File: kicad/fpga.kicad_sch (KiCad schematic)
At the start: 55 parts, among them J3 TC2050 JTAG, J4 SMA 10MHz REF, J5 PMOD0, J6 PMOD1, U10 W25Q128JVSIQ, U12 LFE5U-25F-6BG256C, U14 74LVC1G17

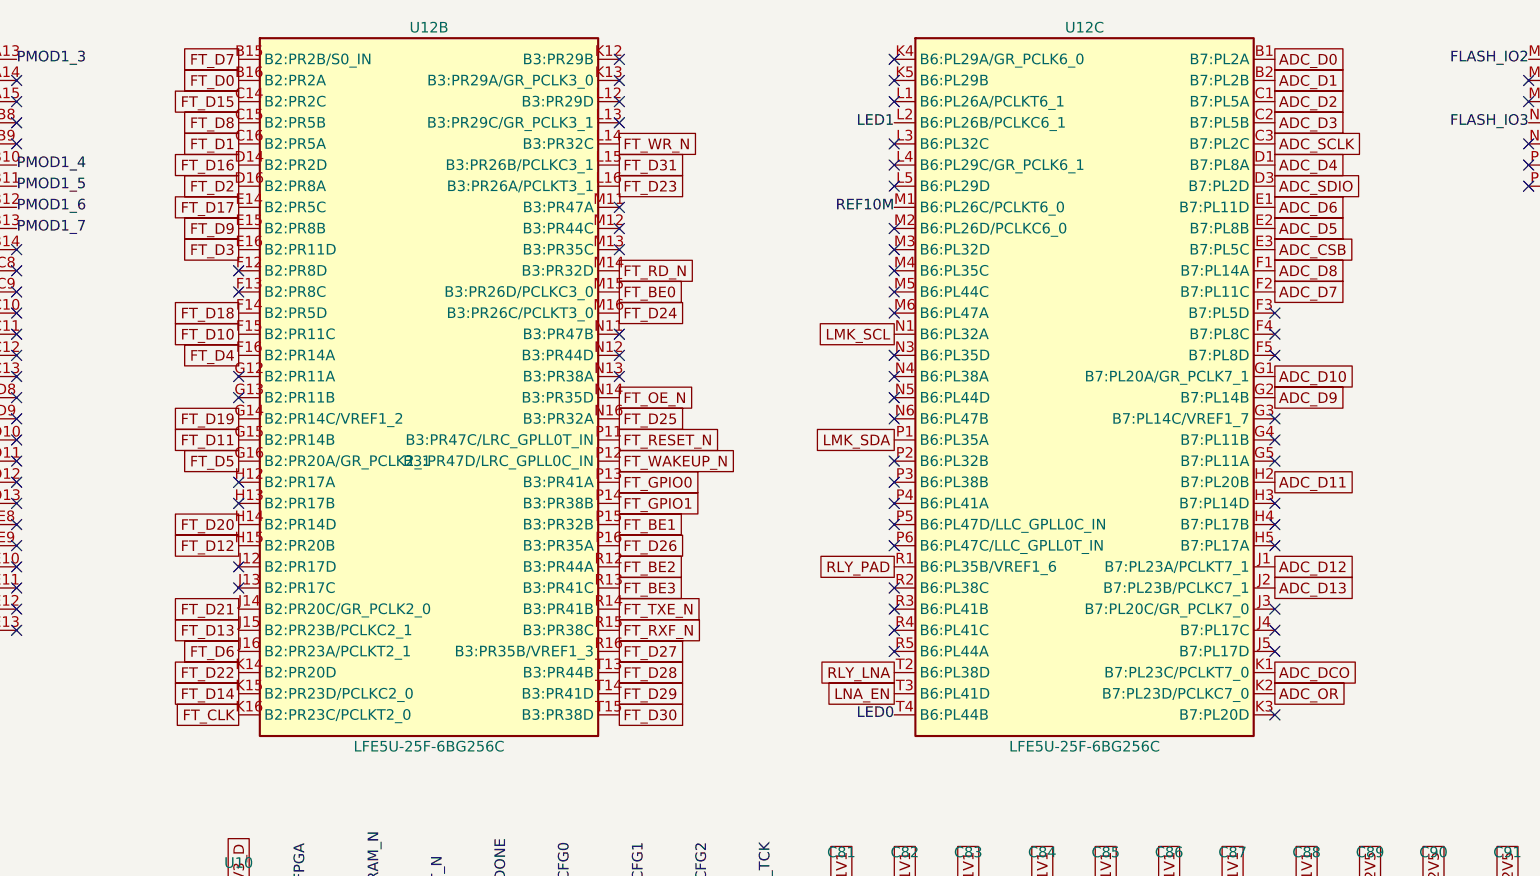
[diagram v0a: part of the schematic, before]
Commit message: Bus pin swap, FT601 IO registers, ADC clock layout, working board and fan-out tooling
- FPGA ball re-assignment (AGY, verified): FT601 and ADC buses planar; LPF, design.py, schematic, netlist synced.
- Gateware: FT601 outputs/tristates in IOLOGIC on a +112.5 deg PLL clock; AD9649 DCO inverted at boot.
- ADC sample clock laid out on F.Cu with swapped polarity; BOM U9 corrected to the 8-pin I2C LMK61E2.
- kicad/work: DeepPCB run 2 board plus scripted patches (buck, In2 GND fill, VCCAUX, clock); DeepPCB snapshots.
- kicad/gen: patch, repair, routing and fan-out scripts (fanout_apply, fanout_trial, place_free, escape_apply).
- notes/pinswap, notes/fanout: briefs, AGY results and Claude's reviews.
- Vendor datasheets removed from the repo; refs/datasheets.md lists their sources.

Co-Authored-By: Claude Opus 5.5 <noreply@anthropic.com>
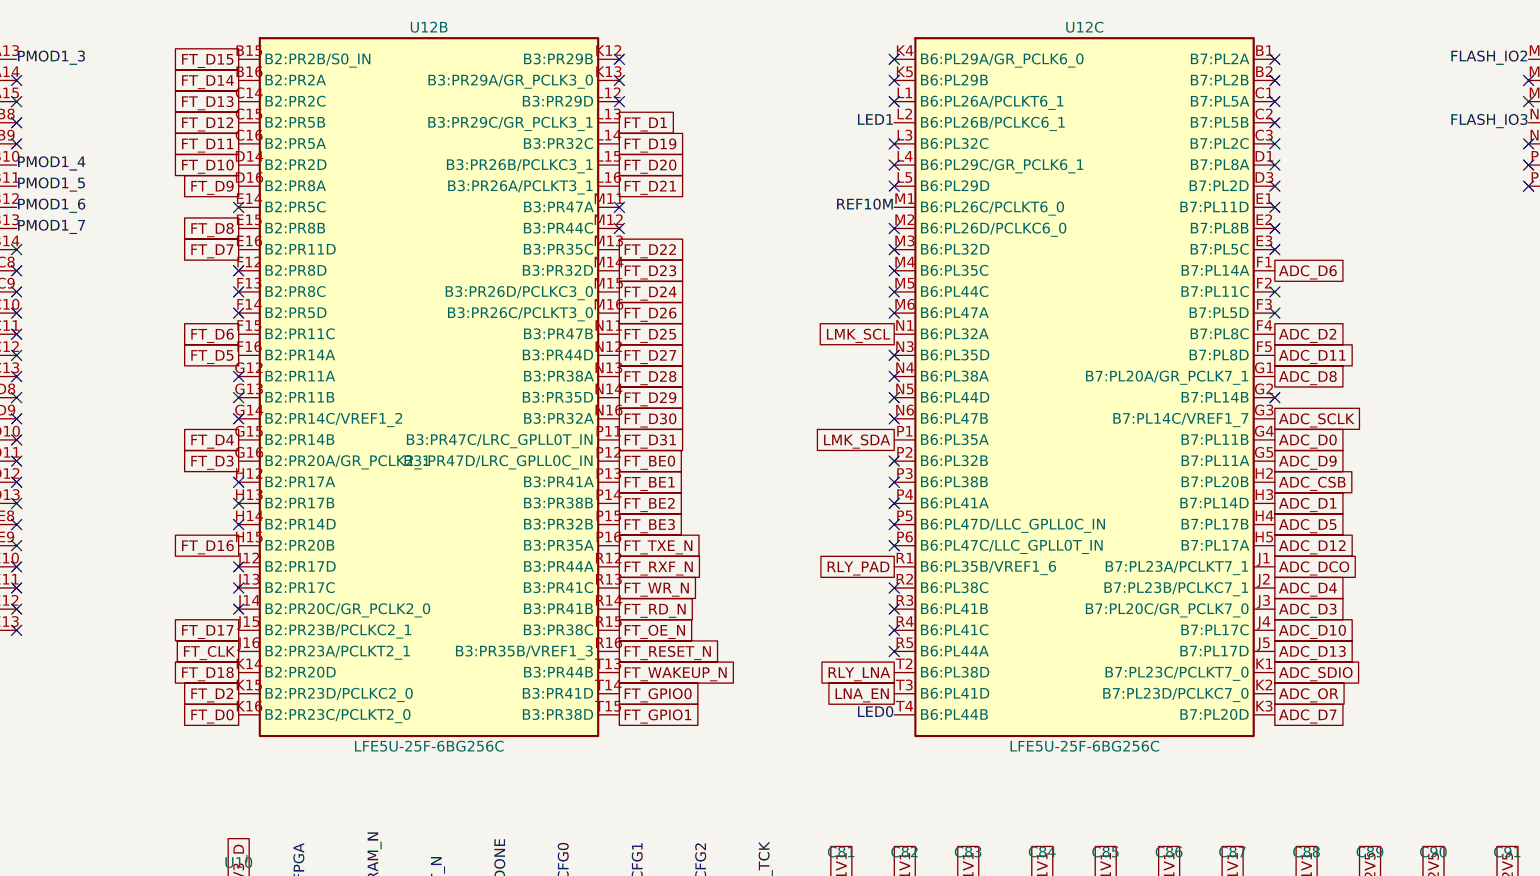
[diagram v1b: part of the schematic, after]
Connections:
- net ADC_CSB: now also U12.H2 (B7:PL20B); no longer U12.E3 (B7:PL5C)
- net ADC_D0: now also U12.G4 (B7:PL11B); no longer U12.B1 (B7:PL2A)
- net ADC_D1: now also U12.H3 (B7:PL14D); no longer U12.B2 (B7:PL2B)
- net ADC_D10: now also U12.J4 (B7:PL17C); no longer U12.G1 (B7:PL20A/GR_PCLK7_1)
- net ADC_D11: now also U12.F5 (B7:PL8D); no longer U12.H2 (B7:PL20B)
- net ADC_D12: now also U12.H5 (B7:PL17A); no longer U12.J1 (B7:PL23A/PCLKT7_1)
- net ADC_D13: now also U12.J5 (B7:PL17D); no longer U12.J2 (B7:PL23B/PCLKC7_1)
- net ADC_D2: now also U12.F4 (B7:PL8C); no longer U12.C1 (B7:PL5A)
- net ADC_D3: now also U12.J3 (B7:PL20C/GR_PCLK7_0); no longer U12.C2 (B7:PL5B)
- net ADC_D4: now also U12.J2 (B7:PL23B/PCLKC7_1); no longer U12.D1 (B7:PL8A)
- net ADC_D5: now also U12.H4 (B7:PL17B); no longer U12.E2 (B7:PL8B)
- net ADC_D6: now also U12.F1 (B7:PL14A); no longer U12.E1 (B7:PL11D)
- net ADC_D7: now also U12.K3 (B7:PL20D); no longer U12.F2 (B7:PL11C)
- net ADC_D8: now also U12.G1 (B7:PL20A/GR_PCLK7_1); no longer U12.F1 (B7:PL14A)
- net ADC_D9: now also U12.G5 (B7:PL11A); no longer U12.G2 (B7:PL14B)
- net ADC_DCO: now also U12.J1 (B7:PL23A/PCLKT7_1); no longer U12.K1 (B7:PL23C/PCLKT7_0)
- net ADC_SCLK: now also U12.G3 (B7:PL14C/VREF1_7); no longer U12.C3 (B7:PL2C)
- net ADC_SDIO: now also U12.K1 (B7:PL23C/PCLKT7_0); no longer U12.D3 (B7:PL2D)
- net FT_BE0: now also U12.P12 (B3:PR47D/LRC_GPLL0C_IN); no longer U12.M15 (B3:PR26D/PCLKC3_0)
- net FT_BE1: now also U12.P13 (B3:PR41A); no longer U12.P15 (B3:PR32B)
- net FT_BE2: now also U12.P14 (B3:PR38B); no longer U12.R12 (B3:PR44A)
- net FT_BE3: now also U12.P15 (B3:PR32B); no longer U12.R13 (B3:PR41C)
- net FT_CLK: now also U12.J16 (B2:PR23A/PCLKT2_1); no longer U12.K16 (B2:PR23C/PCLKT2_0)
- net FT_D0: now also U12.K16 (B2:PR23C/PCLKT2_0); no longer U12.B16 (B2:PR2A)
- net FT_D1: now also U12.L13 (B3:PR29C/GR_PCLK3_1); no longer U12.C16 (B2:PR5A)
- net FT_D10: now also U12.D14 (B2:PR2D); no longer U12.F15 (B2:PR11C)
- net FT_D11: now also U12.C16 (B2:PR5A); no longer U12.G15 (B2:PR14B)
- net FT_D12: now also U12.C15 (B2:PR5B); no longer U12.H15 (B2:PR20B)
- net FT_D13: now also U12.C14 (B2:PR2C); no longer U12.J15 (B2:PR23B/PCLKC2_1)
- net FT_D14: now also U12.B16 (B2:PR2A); no longer U12.K15 (B2:PR23D/PCLKC2_0)
- net FT_D15: now also U12.B15 (B2:PR2B/S0_IN); no longer U12.C14 (B2:PR2C)
- net FT_D16: now also U12.H15 (B2:PR20B); no longer U12.D14 (B2:PR2D)
- net FT_D17: now also U12.J15 (B2:PR23B/PCLKC2_1); no longer U12.E14 (B2:PR5C)
- net FT_D18: now also U12.K14 (B2:PR20D); no longer U12.F14 (B2:PR5D)
- net FT_D19: now also U12.L14 (B3:PR32C); no longer U12.G14 (B2:PR14C/VREF1_2)
- net FT_D2: now also U12.K15 (B2:PR23D/PCLKC2_0); no longer U12.D16 (B2:PR8A)
- net FT_D20: now also U12.L15 (B3:PR26B/PCLKC3_1); no longer U12.H14 (B2:PR14D)
- net FT_D21: now also U12.L16 (B3:PR26A/PCLKT3_1); no longer U12.J14 (B2:PR20C/GR_PCLK2_0)
- net FT_D22: now also U12.M13 (B3:PR35C); no longer U12.K14 (B2:PR20D)
- net FT_D23: now also U12.M14 (B3:PR32D); no longer U12.L16 (B3:PR26A/PCLKT3_1)
- net FT_D24: now also U12.M15 (B3:PR26D/PCLKC3_0); no longer U12.M16 (B3:PR26C/PCLKT3_0)
- net FT_D25: now also U12.N11 (B3:PR47B); no longer U12.N16 (B3:PR32A)
- net FT_D26: now also U12.M16 (B3:PR26C/PCLKT3_0); no longer U12.P16 (B3:PR35A)
- net FT_D27: now also U12.N12 (B3:PR44D); no longer U12.R16 (B3:PR35B/VREF1_3)
- net FT_D28: now also U12.N13 (B3:PR38A); no longer U12.T13 (B3:PR44B)
- net FT_D29: now also U12.N14 (B3:PR35D); no longer U12.T14 (B3:PR41D)
- net FT_D3: now also U12.G16 (B2:PR20A/GR_PCLK2_1); no longer U12.E16 (B2:PR11D)
- net FT_D30: now also U12.N16 (B3:PR32A); no longer U12.T15 (B3:PR38D)
- net FT_D31: now also U12.P11 (B3:PR47C/LRC_GPLL0T_IN); no longer U12.L15 (B3:PR26B/PCLKC3_1)
- net FT_D4: now also U12.G15 (B2:PR14B); no longer U12.F16 (B2:PR14A)
- net FT_D5: now also U12.F16 (B2:PR14A); no longer U12.G16 (B2:PR20A/GR_PCLK2_1)
- net FT_D6: now also U12.F15 (B2:PR11C); no longer U12.J16 (B2:PR23A/PCLKT2_1)
- net FT_D7: now also U12.E16 (B2:PR11D); no longer U12.B15 (B2:PR2B/S0_IN)
- net FT_D8: now also U12.E15 (B2:PR8B); no longer U12.C15 (B2:PR5B)
- net FT_D9: now also U12.D16 (B2:PR8A); no longer U12.E15 (B2:PR8B)
- net FT_GPIO0: now also U12.T14 (B3:PR41D); no longer U12.P13 (B3:PR41A)
- net FT_GPIO1: now also U12.T15 (B3:PR38D); no longer U12.P14 (B3:PR38B)
- net FT_OE_N: now also U12.R15 (B3:PR38C); no longer U12.N14 (B3:PR35D)
- net FT_RD_N: now also U12.R14 (B3:PR41B); no longer U12.M14 (B3:PR32D)
- net FT_RESET_N: now also U12.R16 (B3:PR35B/VREF1_3); no longer U12.P11 (B3:PR47C/LRC_GPLL0T_IN)
- net FT_RXF_N: now also U12.R12 (B3:PR44A); no longer U12.R15 (B3:PR38C)
- net FT_TXE_N: now also U12.P16 (B3:PR35A); no longer U12.R14 (B3:PR41B)
- net FT_WAKEUP_N: now also U12.T13 (B3:PR44B); no longer U12.P12 (B3:PR47D/LRC_GPLL0C_IN)
- net FT_WR_N: now also U12.R13 (B3:PR41C); no longer U12.L14 (B3:PR32C)
